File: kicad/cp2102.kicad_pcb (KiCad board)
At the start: 2 copper layers, 6 parts, among them CON1 USB-MINI-B, P1 CONN_6, U1 CP2102

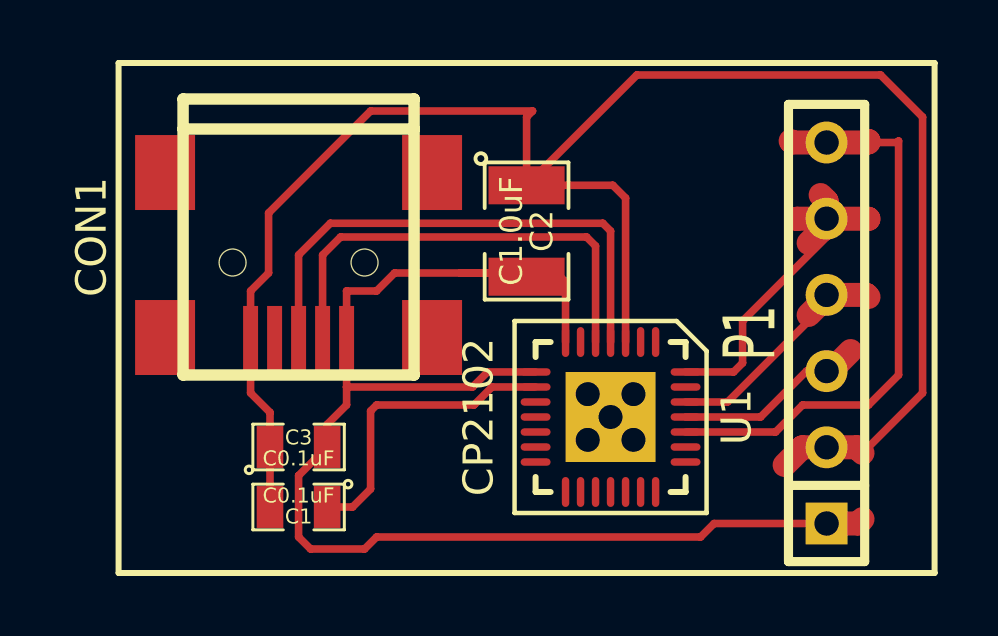
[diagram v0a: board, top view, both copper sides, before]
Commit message: Swpan power pins.
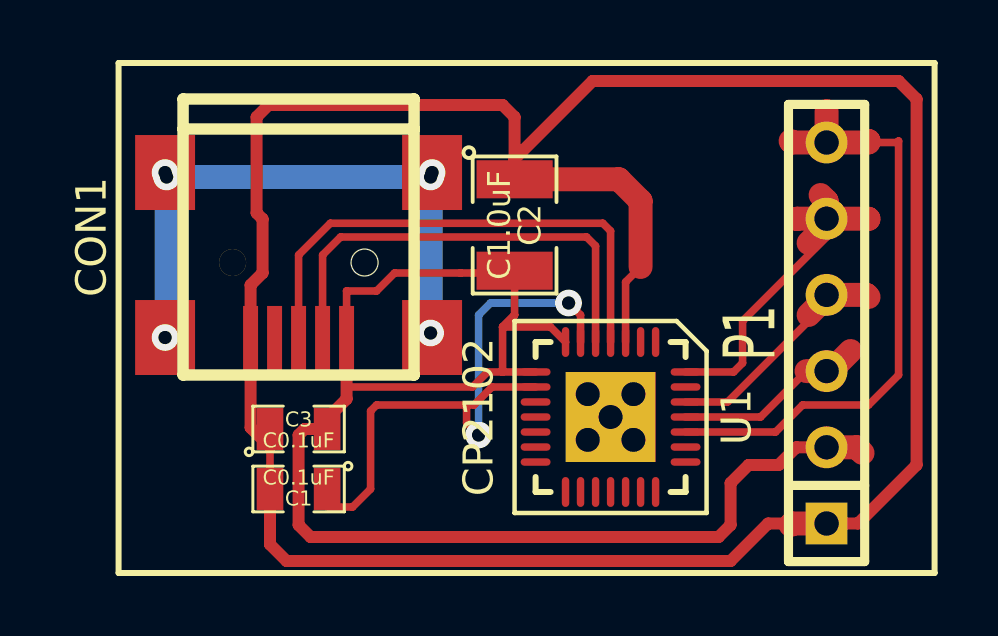
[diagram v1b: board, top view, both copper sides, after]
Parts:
- moved C1 0.60 mm to (151.0, 134.4)
- moved C3 0.60 mm to (151.0, 132.4)
- moved C2 0.45 mm to (158.2, 125.6)
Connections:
- P1 pad 1: /VBUS -> GND
- P1 pad 2: GND -> /VBUS
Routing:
- net GND: track 62.7 -> 86.6 mm
- net N-0000028: track 0.00 -> 20.2 mm, vias 0 -> 6
- net /VDD: track 10.1 -> 19.9 mm, vias 0 -> 2
- net /VBUS: track 46.7 -> 50.8 mm
- net /R: track 20.8 -> 21.8 mm
- net /RX: track 6.41 -> 7.08 mm
